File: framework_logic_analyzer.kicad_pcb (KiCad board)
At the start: 4 copper layers, 26 x 30 mm, 93 parts, among them IC1 TXU0104QWBQARQ1, IC2 TXU0104QWBQARQ1, IC3 TXU0104QWBQARQ1, IC4 TXU0104QWBQARQ1, IC5 CYUSB3014-BZXC, J1 Conn_02x08_Odd_Even, J2 Conn_02x08_Odd_Even, J3 Conn_ARM_JTAG_SWD_10, P1 USB_C_Plug, Q1 MMBT3904, Q2 MMBT3904, Q3 MMBT3904, U1 NCP360SNT1G, U2 WE-TVS-82400102, U3 AP2112K-3.3, U4 SC189CSKTRT, U5 M24M02-DR, Y1 19.200 MHz

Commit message: New header and enclosure
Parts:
- J1, J2: footprint Connector_PinSocket_1.27mm:PinSocket_2x08_P1.27mm_Horizontal -> 20021311-00016T4LF:20021311-00016T4LF
- moved J2 6.19 mm to (143.6, 95.7), turned to 180 degrees
- moved J1 3.13 mm to (128.8, 95.7), turned to 180 degrees
- moved IC1 0.40 mm to (130.2, 91.0)
- moved IC2 0.40 mm to (134.2, 91.0)
- moved IC3 0.40 mm to (138.2, 91.0)
- moved IC4 0.40 mm to (142.2, 91.0)
- moved R4 0.31 mm to (144.8, 91.6)
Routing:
- net GND: track 76.5 -> 94.2 mm, vias 66 -> 82
- net /CH15: track 4.43 -> 6.91 mm
- net /CH13: track 2.89 -> 5.21 mm
- net /CH10: track 2.37 -> 4.68 mm
- net /CH2: track 2.43 -> 4.70 mm
- net /CH0: track 4.02 -> 6.15 mm
- net /CH12: track 2.44 -> 4.56 mm
- net /CH1: track 3.45 -> 5.51 mm
- net /CH14: track 3.90 -> 5.93 mm
- net /CH5: track 2.43 -> 4.39 mm
- net /CH4: track 2.94 -> 4.85 mm
- net /CH11: track 3.61 -> 5.45 mm
- net /CH3: track 2.24 -> 3.93 mm
- net /CH9: track 2.31 -> 3.91 mm
- net /CH6: track 2.11 -> 3.62 mm
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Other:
- outline, holes or cut-outs redrawn
- board text added: "3V3"
- board text added: "BOTTOM SIDE"
- board text added: "GND"
- board text added: "MS CK DO DI RST"
- board text added: "Rev.0"

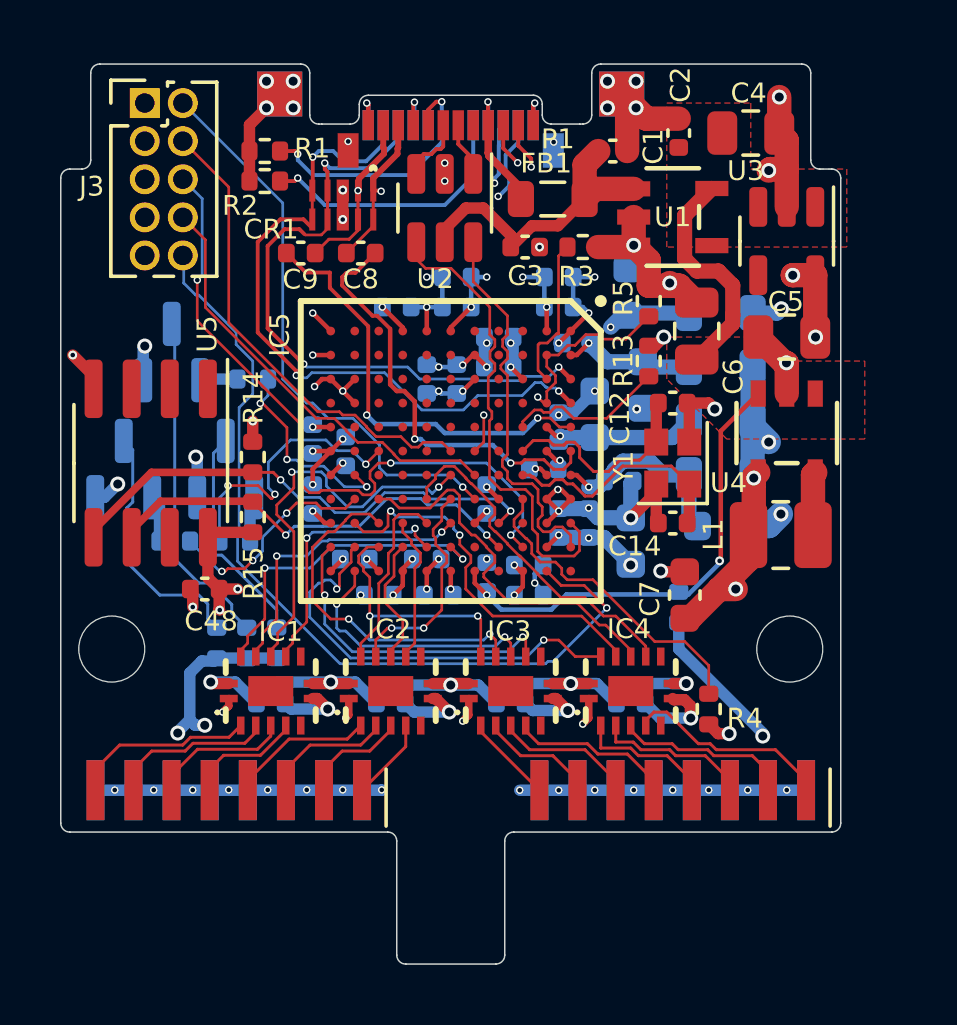
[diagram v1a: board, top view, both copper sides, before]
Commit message: Remove jtag header, add reset button
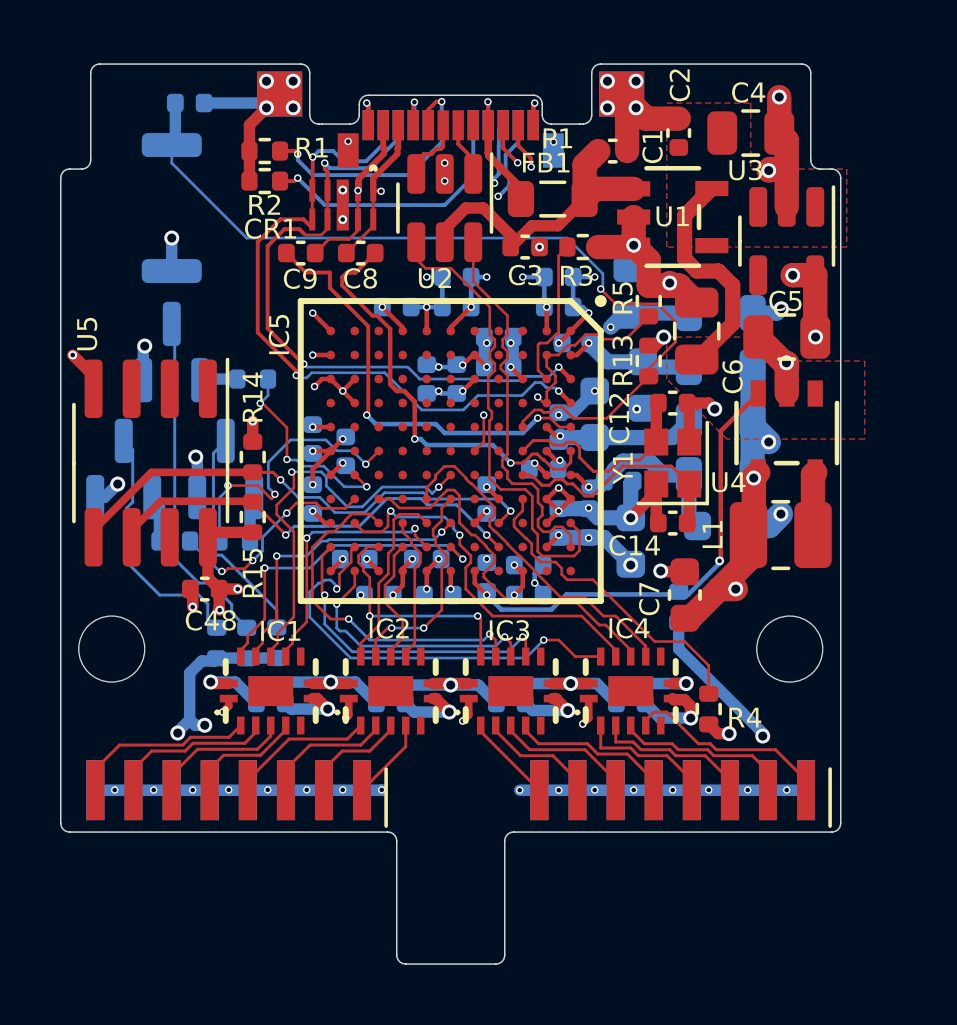
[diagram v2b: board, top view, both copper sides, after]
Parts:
- removed J3: Conn_ARM_JTAG_SWD_10, Connector_PinHeader_1.27mm:PinHeader_2x05_P1.27mm_Vertical
- added C11: 100n, Capacitor_SMD:C_0402_1005Metric, B.Cu at (127.5, 71.4)
- added SW1: SW_Push, Button_Switch_SMD:SW_Push_SPST_NO_Alps_SKRK, B.Cu at (126.9, 74.9)
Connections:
- IC5 pad B11: Net-(IC5-TRST#) -> unconnected-(IC5-TRST#-PadB11)
- IC5 pad C10: Net-(IC5-TDO) -> unconnected-(IC5-TDO-PadC10)
- IC5 pad E7: Net-(IC5-TDI) -> unconnected-(IC5-TDI-PadE7)
- IC5 pad E8: Net-(IC5-TMS) -> unconnected-(IC5-TMS-PadE8)
- IC5 pad F6: Net-(IC5-TCK) -> unconnected-(IC5-TCK-PadF6)
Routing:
- net Net-(IC5-TRST#): track 28.4 -> 0.00 mm, vias 1 -> 0
- net Net-(IC5-RESET#): track 5.39 -> 28.8 mm, vias 0 -> 1
- net Net-(IC5-TDO): track 23.0 -> 0.00 mm, vias 3 -> 0
- net Net-(IC5-TMS): track 19.1 -> 0.00 mm, vias 1 -> 0
- net Net-(IC5-TCK): track 16.0 -> 0.00 mm
- net Net-(IC5-TDI): track 14.6 -> 0.00 mm
- net GND: track 94.2 -> 97.7 mm, vias 82 -> 83
- net /CH1: track 5.51 -> 4.58 mm
- net /CH6: track 3.62 -> 2.77 mm
- net /CH5: track 4.39 -> 3.54 mm
- net /CH3: track 3.93 -> 3.08 mm
- net /CH14: track 5.93 -> 5.14 mm
- net /CH0: track 6.15 -> 5.45 mm
- net /CH15: track 6.91 -> 6.40 mm
- net /CH9: track 3.91 -> 3.41 mm
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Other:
- board text removed: "3V3"
- board text removed: "GND"
- board text removed: "MS CK DO DI RST"

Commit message: fixed things
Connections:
- net +3V3 renamed +3.3V
